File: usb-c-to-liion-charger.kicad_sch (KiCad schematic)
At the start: 3 parts

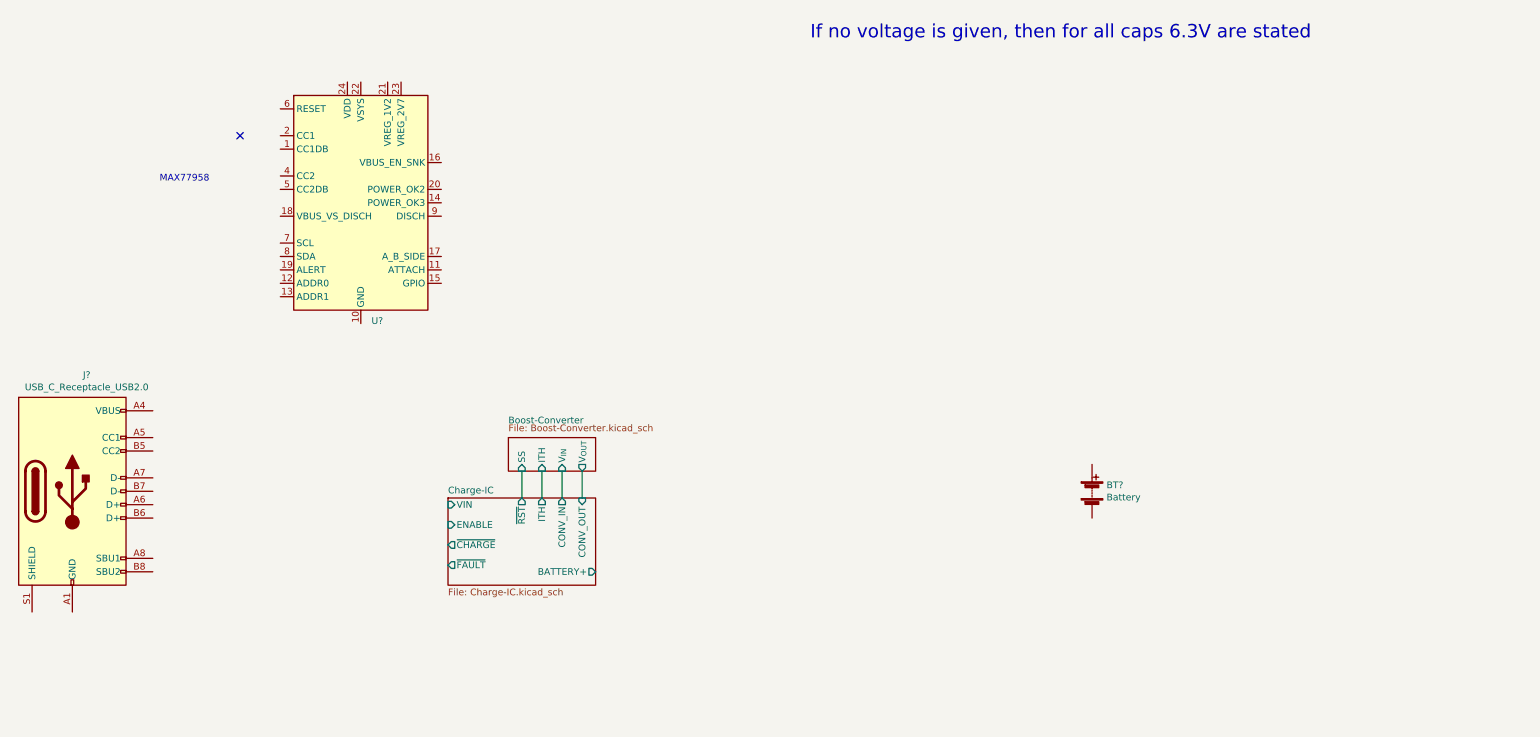
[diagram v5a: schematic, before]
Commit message: Finish schematic
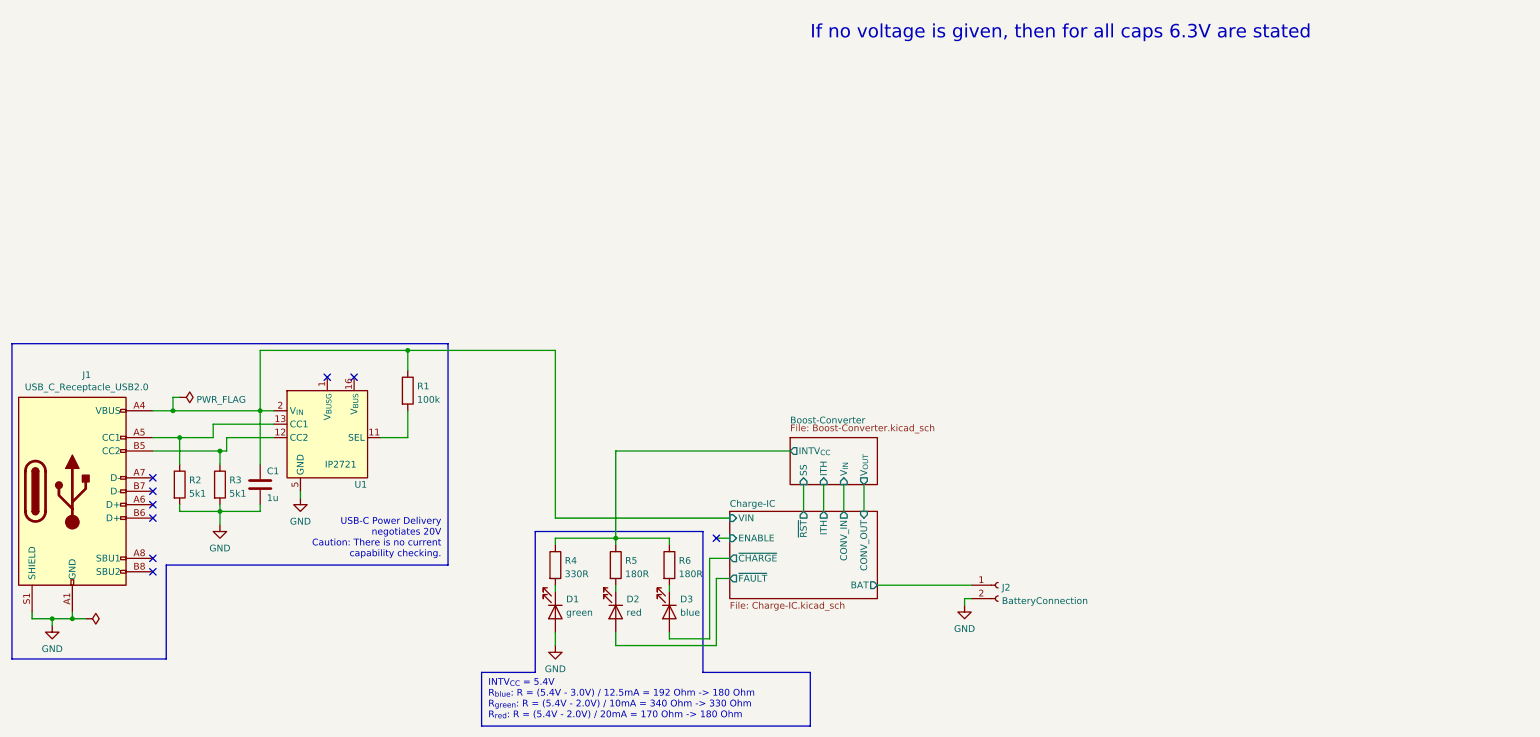
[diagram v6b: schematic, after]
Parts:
- removed BT?: Battery, symbol Device:Battery
- removed U?: (no value), symbol Interface_USB:STUSB4500QTR
- added C1: 1u, symbol Device:C
- added D1: green, symbol Device:LED
- added D2: red, symbol Device:LED
- added D3: blue, symbol Device:LED
- added J2: BatteryConnection, symbol Connector:Conn_01x02_Female
- added R1: 100k, symbol Device:R
- added R2, R3: 5k1, symbol Device:R
- added R4: 330R, symbol Device:R
- added R5, R6: 180R, symbol Device:R
- added U1: IP2721, Package_SO:TSSOP-16_4.4x5mm_P0.65mm, symbol extraSymbols:IP2721
- J1: renamed from J?; footprint (none) -> Connector_USB:USB_C_Receptacle_Palconn_UTC16-G
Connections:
- net Charge-IC/VIN: now also J1.A4 (VBUS), J1.A9 (VBUS), J1.B4 (VBUS), J1.B9 (VBUS), C1.1, R1.1, U1.2 (V_{IN})
- net Charge-IC/~{CHARGE}: now also D3.2 (A)
- net Charge-IC/~{FAULT}: now also D2.2 (A)
- net GND: now reaches J1.A1 (GND), J1.A12 (GND), J1.B1 (GND), J1.B12 (GND)
- net GND: now also J1.S1 (SHIELD), C1.2, D1.2 (A), J2.2 (Pin_2), R2.2, R3.2, U1.5 (GND)
- net at J1.A5 (CC1): now also R2.1, U1.13 (CC1)
- net at J1.B5 (CC2): now also R3.1, U1.12 (CC2)
- new net: D3.1 (K), R6.2
- new net: D2.1 (K), R5.2
- new net: D1.1 (K), R4.2
- new net: R1.2, U1.11 (SEL)
- new net Boost-Converter/INTV_{CC}: R4.1, R5.1, R6.1
- new net Charge-IC/BAT: J2.1 (Pin_1)
- no-connect marks 1 -> 9
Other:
- sheet Boost-Converter ports: added INTV_{CC}; removed none
- sheet Charge-IC ports: added BAT; removed BATTERY+
- note added: "INTV_{CC} = 5.4V R_{blue}: R = (5.4V - 3.0V) / 12.5mA = 192 Ohm -> 180 Ohm R_{green}: R = (5.4V - 2.0V) / 10mA = 340 Ohm -> 330 Ohm R_{red}: R = (5.4V - 2.0V) / 20mA = 170 Ohm -> 180 Ohm"
- note added: "USB-C Power Delivery negotiates 20V Caution: There is no current capability checking."
- note removed: "MAX77958"

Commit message: Small changes
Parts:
- C1: footprint (none) -> Capacitor_SMD:C_0603_1608Metric
- D1, D2, D3: footprint (none) -> LED_SMD:LED_0603_1608Metric
- R1, R2, R3, R4, R5, R6: footprint (none) -> Resistor_SMD:R_0603_1608Metric
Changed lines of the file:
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@@
       (effects (font (size 1.27 1.27)) (justify left))
     )
-    (property "Footprint" "" (id 2) (at 51.562 102.87 90)
+    (property "Footprint" "Resistor_SMD:R_0603_1608Metric" (id 2) (at 51.562 102.87 90)
       (effects (font (size 1.27 1.27)) hide)
     )
@@
       (effects (font (size 1.27 1.27)) (justify left))
     )
-    (property "Footprint" "" (id 2) (at 144.272 118.11 90)
+    (property "Footprint" "Resistor_SMD:R_0603_1608Metric" (id 2) (at 144.272 118.11 90)
       (effects (font (size 1.27 1.27)) hide)
     )
@@
       (effects (font (size 1.27 1.27)) (justify left))
     )
-    (property "Footprint" "" (id 2) (at 134.112 118.11 90)
+    (property "Footprint" "Resistor_SMD:R_0603_1608Metric" (id 2) (at 134.112 118.11 90)
       (effects (font (size 1.27 1.27)) hide)
     )
@@
       (effects (font (size 1.27 1.27)) (justify left))
     )
-    (property "Footprint" "" (id 2) (at 135.89 127 0)
+    (property "Footprint" "LED_SMD:LED_0603_1608Metric" (id 2) (at 135.89 127 0)
       (effects (font (size 1.27 1.27)) hide)
     )
@@
       (effects (font (size 1.27 1.27)) (justify left))
     )
-    (property "Footprint" "" (id 2) (at 69.5452 106.68 0)
+    (property "Footprint" "Capacitor_SMD:C_0603_1608Metric" (id 2) (at 69.5452 106.68 0)
       (effects (font (size 1.27 1.27)) hide)
     )
@@
       (effects (font (size 1.27 1.27)) (justify left))
     )
-    (property "Footprint" "" (id 2) (at 124.46 127 0)
+    (property "Footprint" "LED_SMD:LED_0603_1608Metric" (id 2) (at 124.46 127 0)
       (effects (font (size 1.27 1.27)) hide)
     )
@@
       (effects (font (size 1.27 1.27)) (justify left))
     )
-    (property "Footprint" "" (id 2) (at 122.682 118.11 90)
+    (property "Footprint" "Resistor_SMD:R_0603_1608Metric" (id 2) (at 122.682 118.11 90)
       (effects (font (size 1.27 1.27)) hide)
     )
@@
       (effects (font (size 1.27 1.27)) hide)
     )
-    (property "Value" "" (id 1) (at 38.735 128.7038 90)
+    (property "Value" "PWR_FLAG" (id 1) (at 38.735 128.7038 90)
       (effects (font (size 1.27 1.27)) (justify left))
     )
@@
       (effects (font (size 1.27 1.27)) (justify left))
     )
-    (property "Footprint" "" (id 2) (at 94.742 85.09 90)
+    (property "Footprint" "Resistor_SMD:R_0603_1608Metric" (id 2) (at 94.742 85.09 90)
       (effects (font (size 1.27 1.27)) hide)
     )
@@
       (effects (font (size 1.27 1.27)) (justify left))
     )
-    (property "Footprint" "" (id 2) (at 59.182 102.87 90)
+    (property "Footprint" "Resistor_SMD:R_0603_1608Metric" (id 2) (at 59.182 102.87 90)
       (effects (font (size 1.27 1.27)) hide)
     )
@@
       (effects (font (size 1.27 1.27)) (justify left))
     )
-    (property "Footprint" "" (id 2) (at 146.05 127 0)
+    (property "Footprint" "LED_SMD:LED_0603_1608Metric" (id 2) (at 146.05 127 0)
       (effects (font (size 1.27 1.27)) hide)
     )
@@
       (reference "#PWR0123") (unit 1) (value "GND") (footprint "")
     )
+    (path "/470ed0ff-c7a4-4f13-ad04-badcdcbc3fb4/56772fef-1036-4cd6-bfe6-4681f93e97b5"
+      (reference "#PWR?") (unit 1) (value "GND") (footprint "")
+    )
+    (path "/470ed0ff-c7a4-4f13-ad04-badcdcbc3fb4/878773f3-9fa2-48f5-a95e-384afd63efc0"
+      (reference "#PWR?") (unit 1) (value "GND") (footprint "")
+    )
+    (path "/470ed0ff-c7a4-4f13-ad04-badcdcbc3fb4/aef7e9e4-2cc7-4441-a86a-d55312de79ad"
+      (reference "#PWR?") (unit 1) (value "GND") (footprint "")
+    )
     (path "/7093c4c0-90b3-4105-b334-f3bf66fa4b35"
       (reference "C1") (unit 1) (value "1u") (footprint "Capacitor_SMD:C_0603_1608Metric")
     )
     (path "/129dbfb3-87d3-4989-9b99-2f3715fc4ca9/b1f560fb-91b8-4a37-a09d-9567928098a4"
-      (reference "C2") (unit 1) (value "~") (footprint "Capacitor_SMD:C_0603_1608Metric")
+      (reference "C2") (unit 1) (value "DNP") (footprint "Capacitor_SMD:C_0603_1608Metric")
     )
     (path "/129dbfb3-87d3-4989-9b99-2f3715fc4ca9/4c3c8e27-44e2-462b-8597-15421e35f084"
@@
     )
     (path "/129dbfb3-87d3-4989-9b99-2f3715fc4ca9/1738e819-c10f-4633-afb8-c84407d6be96"
-      (reference "C4") (unit 1) (value "~") (footprint "Capacitor_SMD:C_0603_1608Metric")
+      (reference "C4") (unit 1) (value "DNP") (footprint "Capacitor_SMD:C_0603_1608Metric")
     )
     (path "/129dbfb3-87d3-4989-9b99-2f3715fc4ca9/f1f40757-99be-430a-a844-42d9f7a7618a"
@@
       (reference "C21") (unit 1) (value "10u") (footprint "Capacitor_SMD:C_0805_2012Metric")
     )
+    (path "/470ed0ff-c7a4-4f13-ad04-badcdcbc3fb4/48814147-ae47-4bf6-b8ec-55c652968cf4"
+      (reference "C?") (unit 1) (value "22u 25V") (footprint "Capacitor_SMD:C_0805_2012Metric")
+    )
+    (path "/470ed0ff-c7a4-4f13-ad04-badcdcbc3fb4/6d589334-ed46-4724-8f6a-46e5f08827d1"
+      (reference "C?") (unit 1) (value "22u 25V") (footprint "Capacitor_SMD:C_0805_2012Metric")
+    )
+    (path "/470ed0ff-c7a4-4f13-ad04-badcdcbc3fb4/db4458ff-9d0e-4dfe-a9ab-b97b1b7ff84f"
+      (reference "C?") (unit 1) (value "22u 25V") (footprint "Capacitor_SMD:C_0805_2012Metric")
+    )
     (path "/8027d007-1af8-4bbf-8136-523258bbebd1"

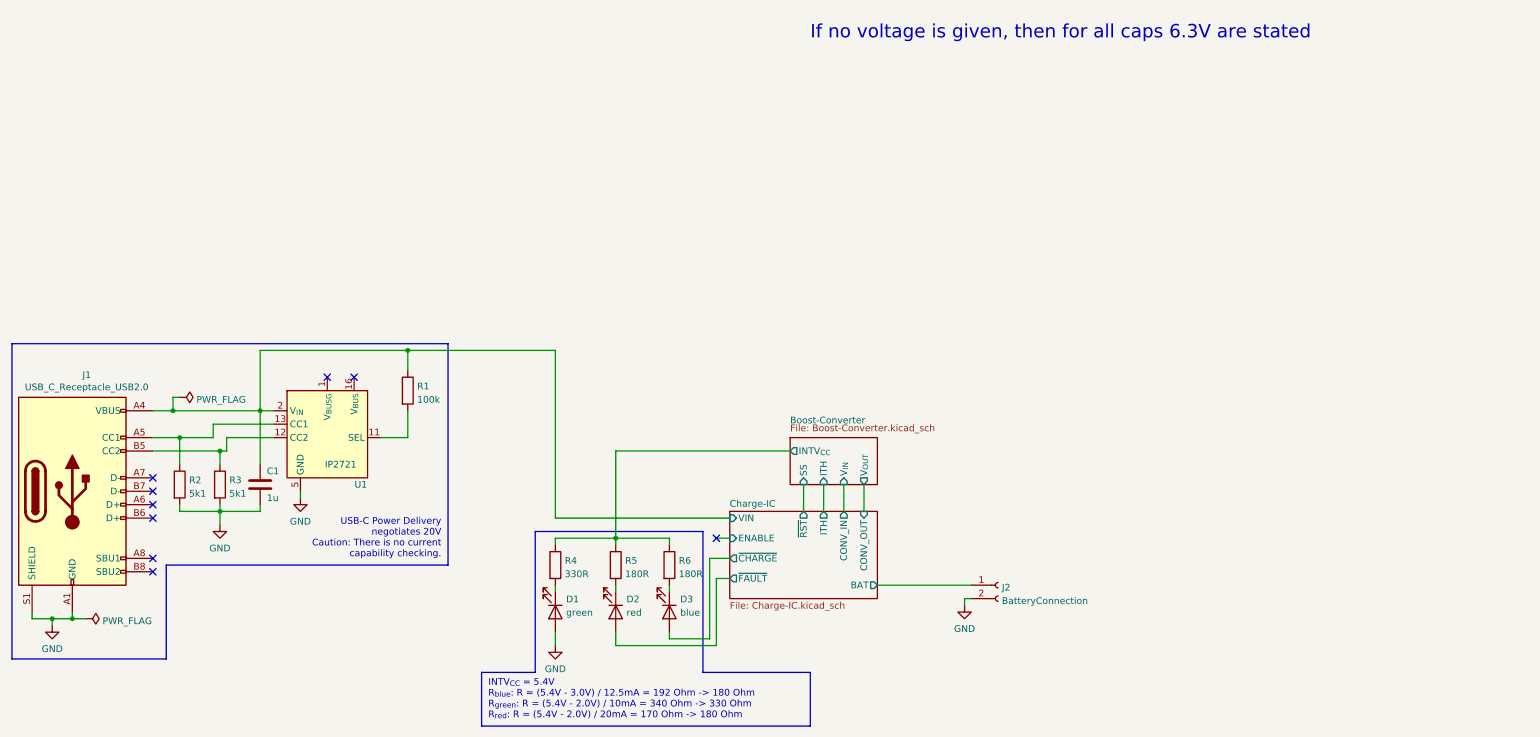
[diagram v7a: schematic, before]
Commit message: Annotate symbols and assign footprints
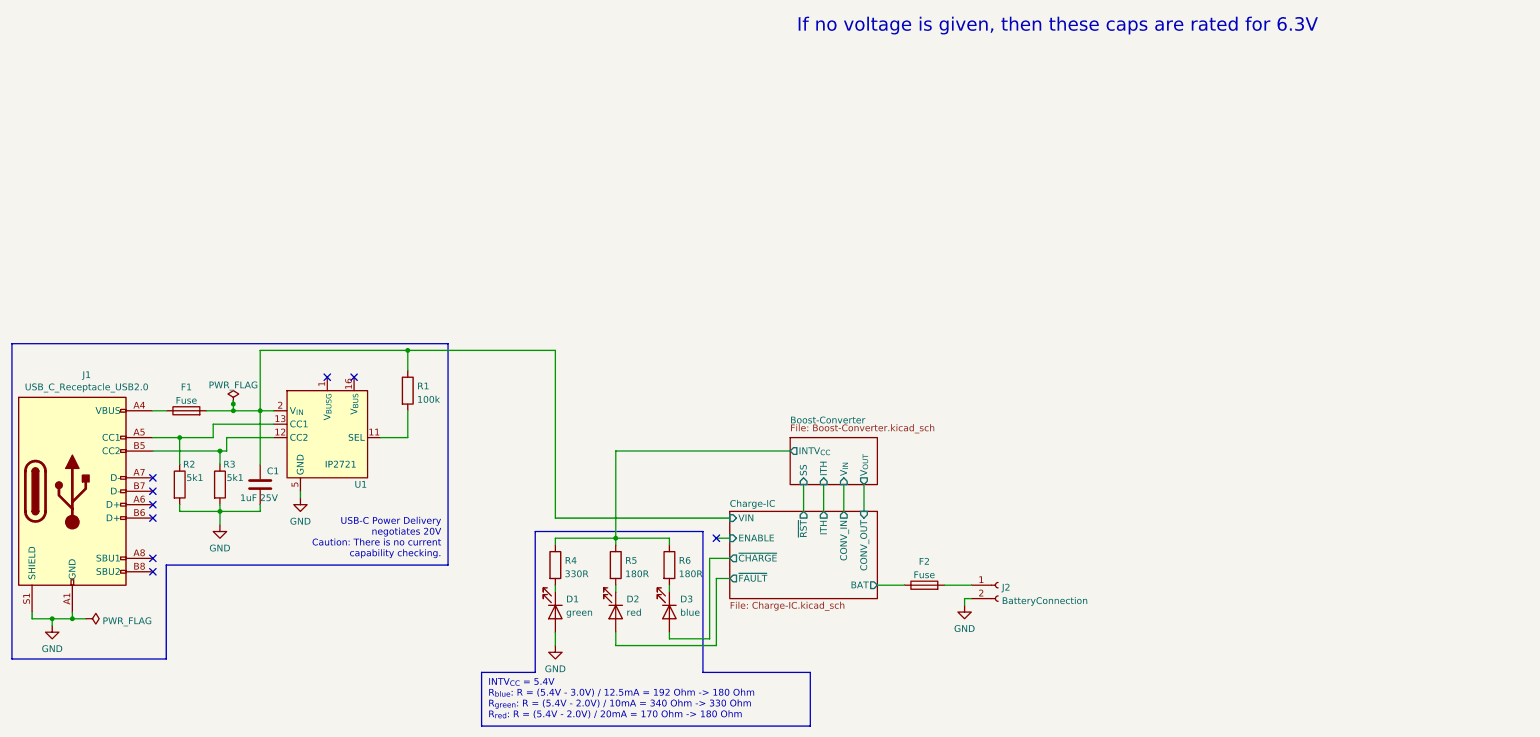
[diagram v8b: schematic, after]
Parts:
- added F1, F2: Fuse, extraFootprints:KEYSTONE-FUSE-3557-2, symbol Device:Fuse
- C1: value 1u -> 1uF 25V
- J2: footprint (none) -> Connector_AMASS:AMASS_XT30U-M_1x02_P5.0mm_Vertical
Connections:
- net Charge-IC/BAT: now also F2.1; no longer J2.1 (Pin_1)
- net Charge-IC/VIN: now also F1.2; no longer J1.A4 (VBUS), J1.A9 (VBUS), J1.B4 (VBUS), J1.B9 (VBUS)
- new net: F1.1, J1.A4 (VBUS), J1.A9 (VBUS), J1.B4 (VBUS), J1.B9 (VBUS)
- new net: F2.2, J2.1 (Pin_1)
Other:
- note added: "If no voltage is given, then these caps are rated for 6.3V"
- note removed: "If no voltage is given, then for all caps 6.3V are stated"
